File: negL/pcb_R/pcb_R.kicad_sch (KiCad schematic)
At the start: 105 parts, among them J1 MJ-4PP-9, J2 FH-1x4SG/RH, J3 XA-3-2-7P, Q1 AO3401A, SW1 TVBP06-B043CB-B, SW2 EVQWGD001, U1 nice_nano, U2 74HC595, U3 AE-XCL103-3V3

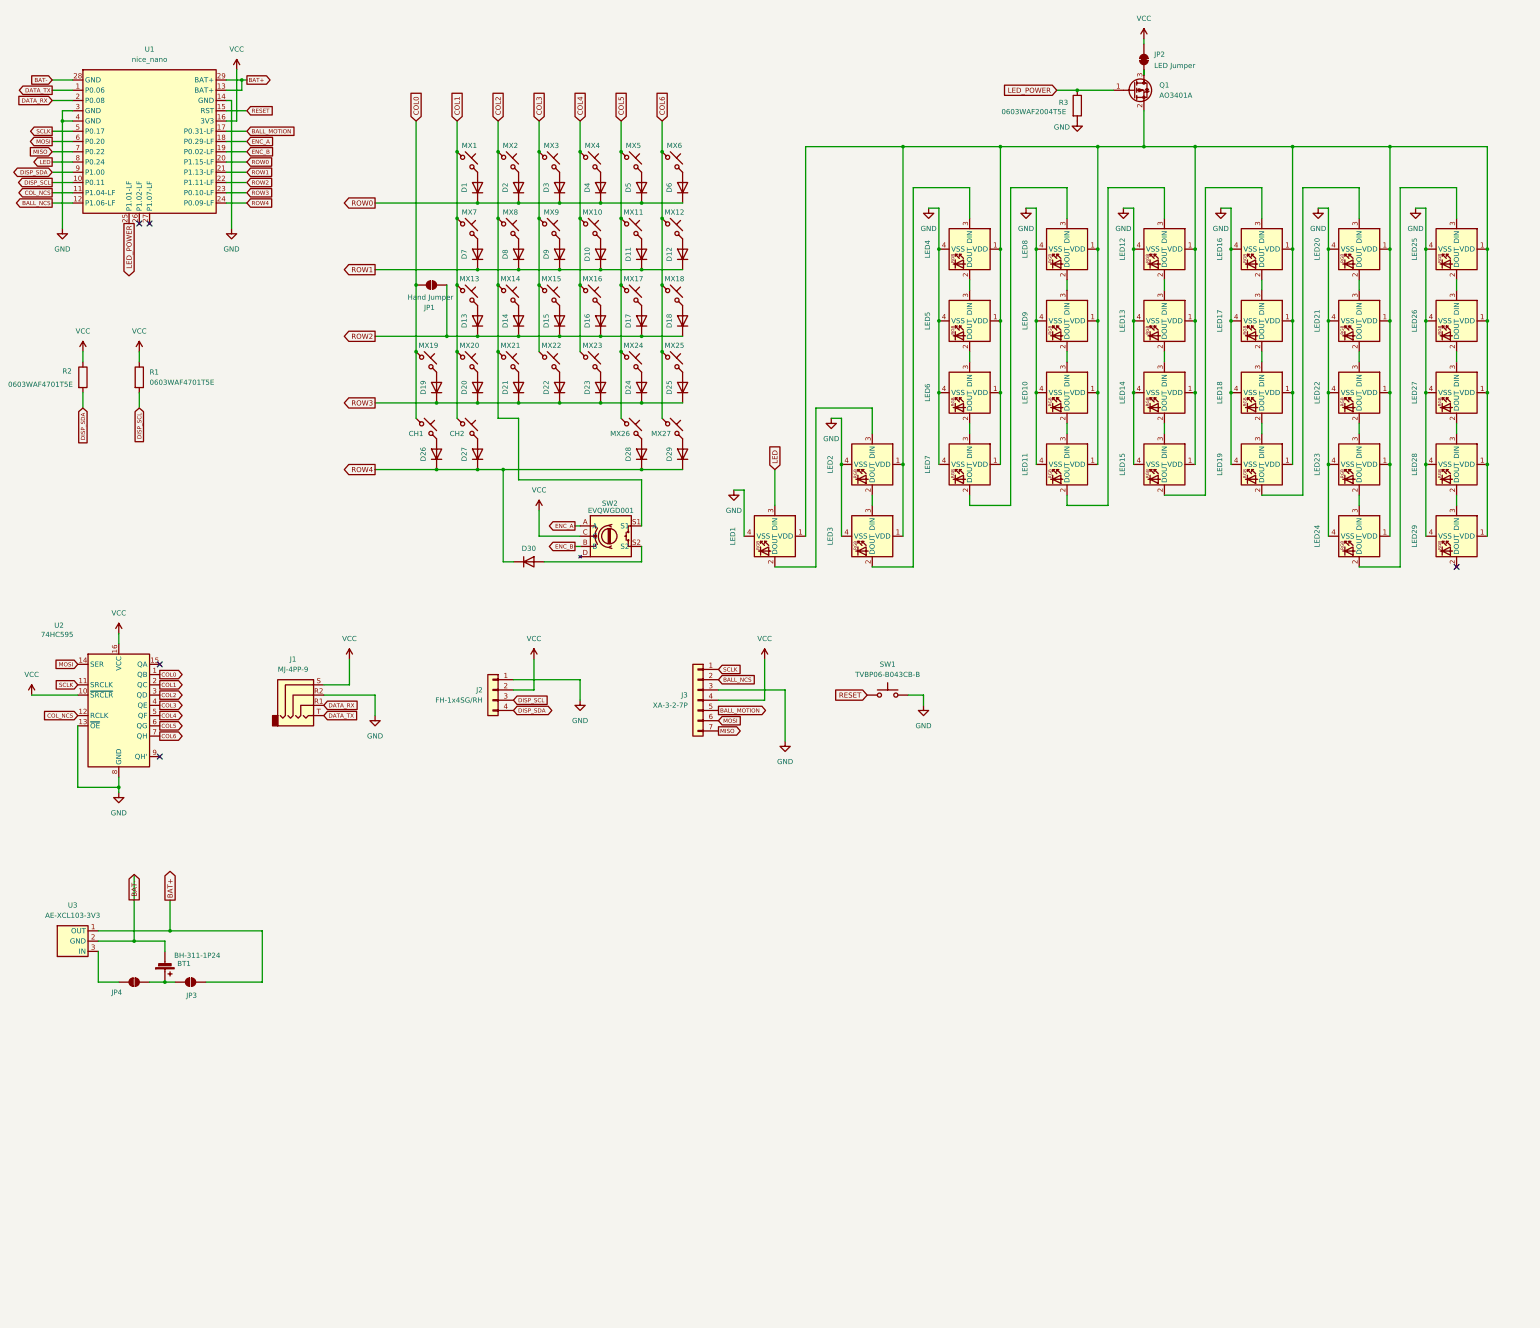
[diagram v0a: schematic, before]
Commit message: Add switches
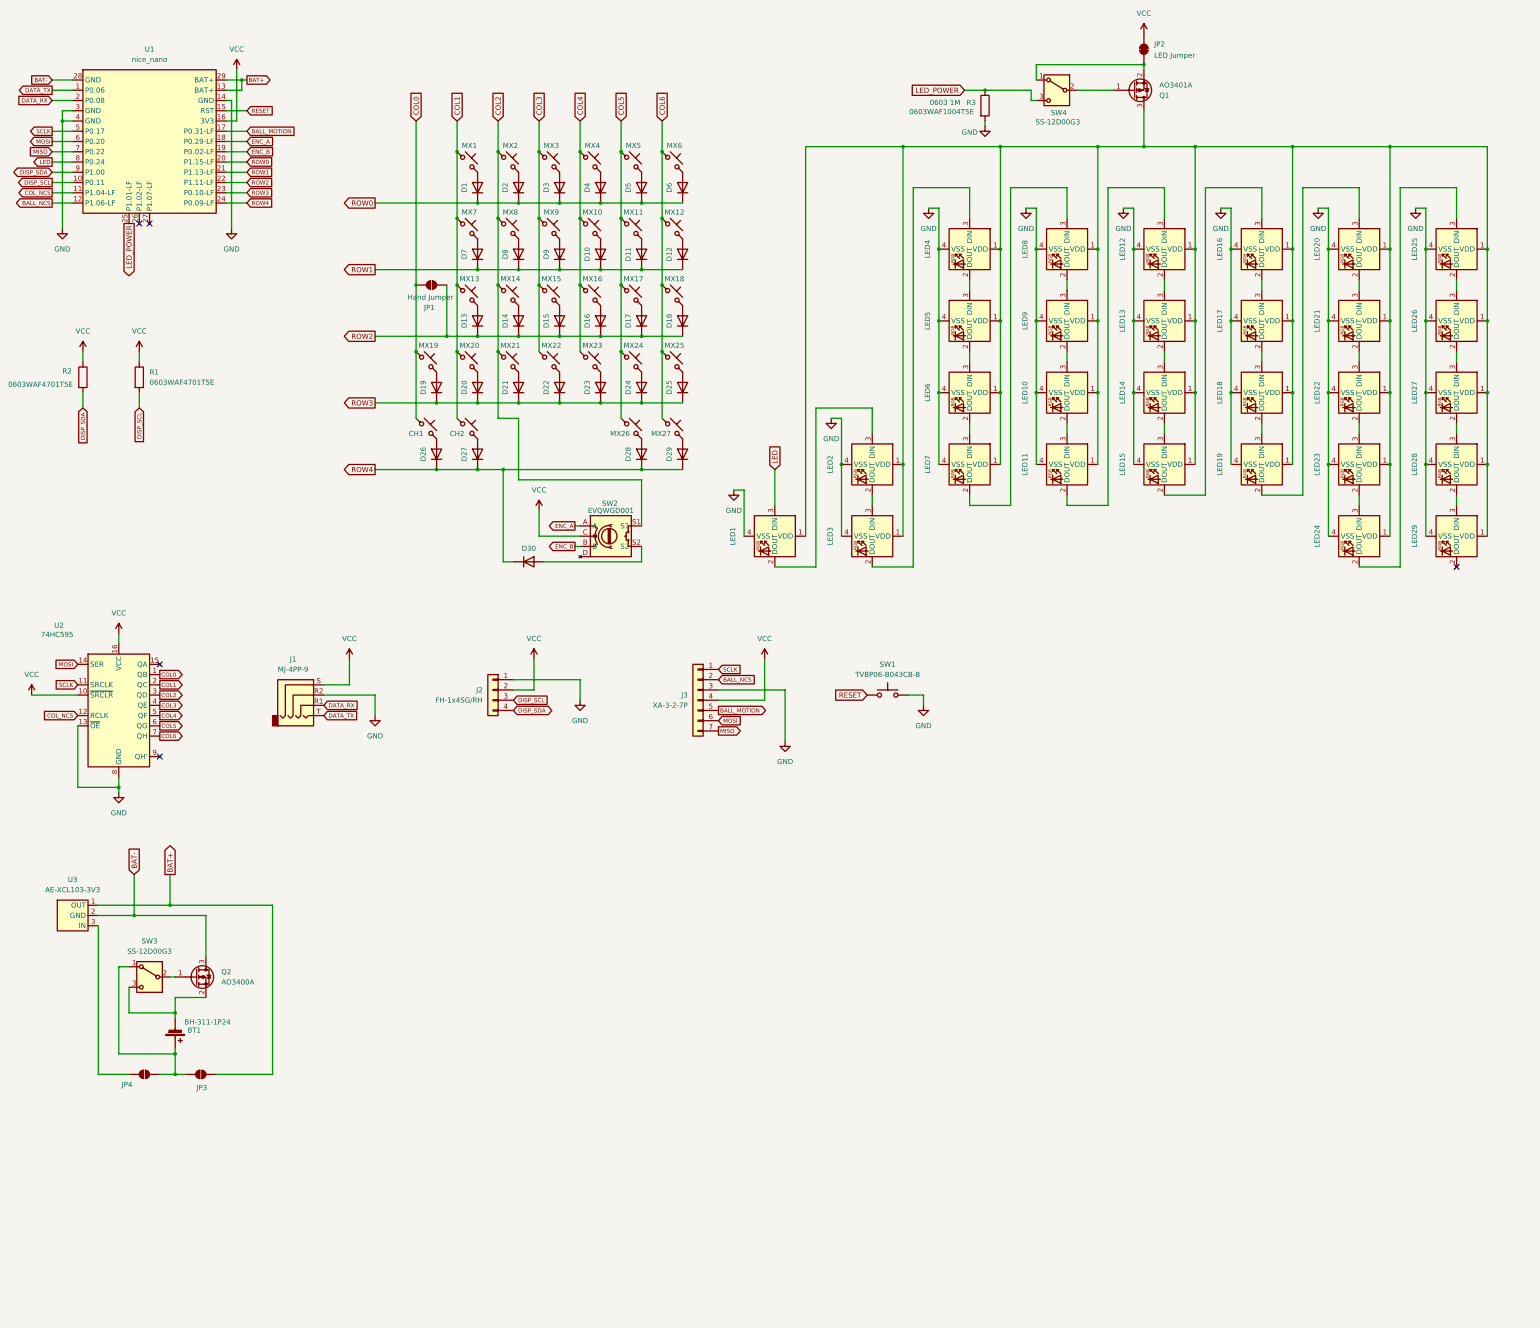
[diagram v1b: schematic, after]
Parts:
- added Q2: AO3400A, Package_TO_SOT_SMD:SOT-23, symbol Transistor_FET:AO3400A
- added SW3, SW4: SS-12D00G3, neg_footprints:SS-12D00G3, symbol Switch:SW_SPDT
- BT1, J1, J2, SW1: now left out of the parts list
- R3: value 0603WAF2004T5E -> 0603WAF1004T5E; LCSC C22976 -> C22935
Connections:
- net BAT-: now also Q2.3 (D); no longer BT1.2 (-)
- net LED_POWER: now also SW4.3 (C); no longer Q1.1 (G)
- net at LED1.1 (VDD), LED10.1 (VDD), LED11.1 (VDD)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: now also Q1.3 (D); no longer Q1.2 (S)
- net at JP2.2 (B): now also Q1.2 (S), SW4.1 (A); no longer Q1.3 (D)
- net at BT1.1 (+), JP3.1 (A), JP4.2 (B): now also SW3.1 (A)
- new net: Q1.1 (G), SW4.2 (B)
- new net: Q2.1 (G), SW3.2 (B)
- new net: BT1.2 (-), Q2.2 (S), SW3.3 (C)
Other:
- moved on the sheet: BT1, JP2, JP3, JP4, R3, U3

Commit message: update
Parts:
- added JP10, JP7, JP8, JP9: ~, Jumper:SolderJumper-2_P1.3mm_Open_Pad1.0x1.5mm, symbol Jumper:SolderJumper_2_Open
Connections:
- net DATA_RX: now also JP10.2 (B), JP7.2 (B); no longer J1.R1
- net DATA_TX: now also JP8.2 (B), JP9.2 (B); no longer J1.T
- new net: J1.R1, JP7.1 (A), JP9.1 (A)
- new net: J1.T, JP10.1 (A), JP8.1 (A)
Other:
- moved on the sheet: J1

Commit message: update
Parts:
- renumbered JP7 to JP5, JP8 to JP6, JP9 to JP7, JP10 to JP8
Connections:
- net COL0: now also U2.15 (QA); no longer MX19.1, U2.1 (QB)
- net COL1: now also MX19.1, U2.1 (QB); no longer MX1.1, MX13.1, MX20.1, MX7.1, U2.2 (QC)
- net COL2: now also MX1.1, MX13.1, MX20.1, MX7.1, U2.2 (QC); no longer MX14.1, MX2.1, MX21.1, MX8.1, U2.3 (QD)
- net COL3: now also MX14.1, MX2.1, MX21.1, MX8.1, U2.3 (QD); no longer MX15.1, MX22.1, MX3.1, MX9.1, U2.4 (QE)
- net COL4: now also MX15.1, MX22.1, MX3.1, MX9.1, U2.4 (QE); no longer MX10.1, MX16.1, MX23.1, MX4.1, U2.5 (QF)
- net COL5: now also MX10.1, MX16.1, MX23.1, MX4.1, U2.5 (QF); no longer MX11.1, MX17.1, MX24.1, MX26.1, MX5.1, U2.6 (QG)
- net COL6: now also MX11.1, MX17.1, MX24.1, MX26.1, MX5.1, U2.6 (QG); no longer MX12.1, MX18.1, MX25.1, MX27.1, MX6.1, U2.7 (QH)
- net ROW2: no longer JP1.2 (B)
- net ROW3: now also JP1.2 (B)
- new net COL7: MX12.1, MX18.1, MX25.1, MX27.1, MX6.1, U2.7 (QH)
- no-connect marks 5 -> 4
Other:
- note added: "JP3: Enables direct output from battery. Intented to use with 14500 battery. JP4: Enables step up converter to 3.3V. Intended to use with normal AA battery."
- note added: "NOTE: XCL103's max current is 0.25A at 1.5V, which is not enough to light all LEDs in max brightness"
- note added: "Short JP7 and JP8 for right hand"
- moved on the sheet: BT1, D30, J1, J2, J3, JP3, JP4, JP5, JP6, JP7, JP8, Q2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

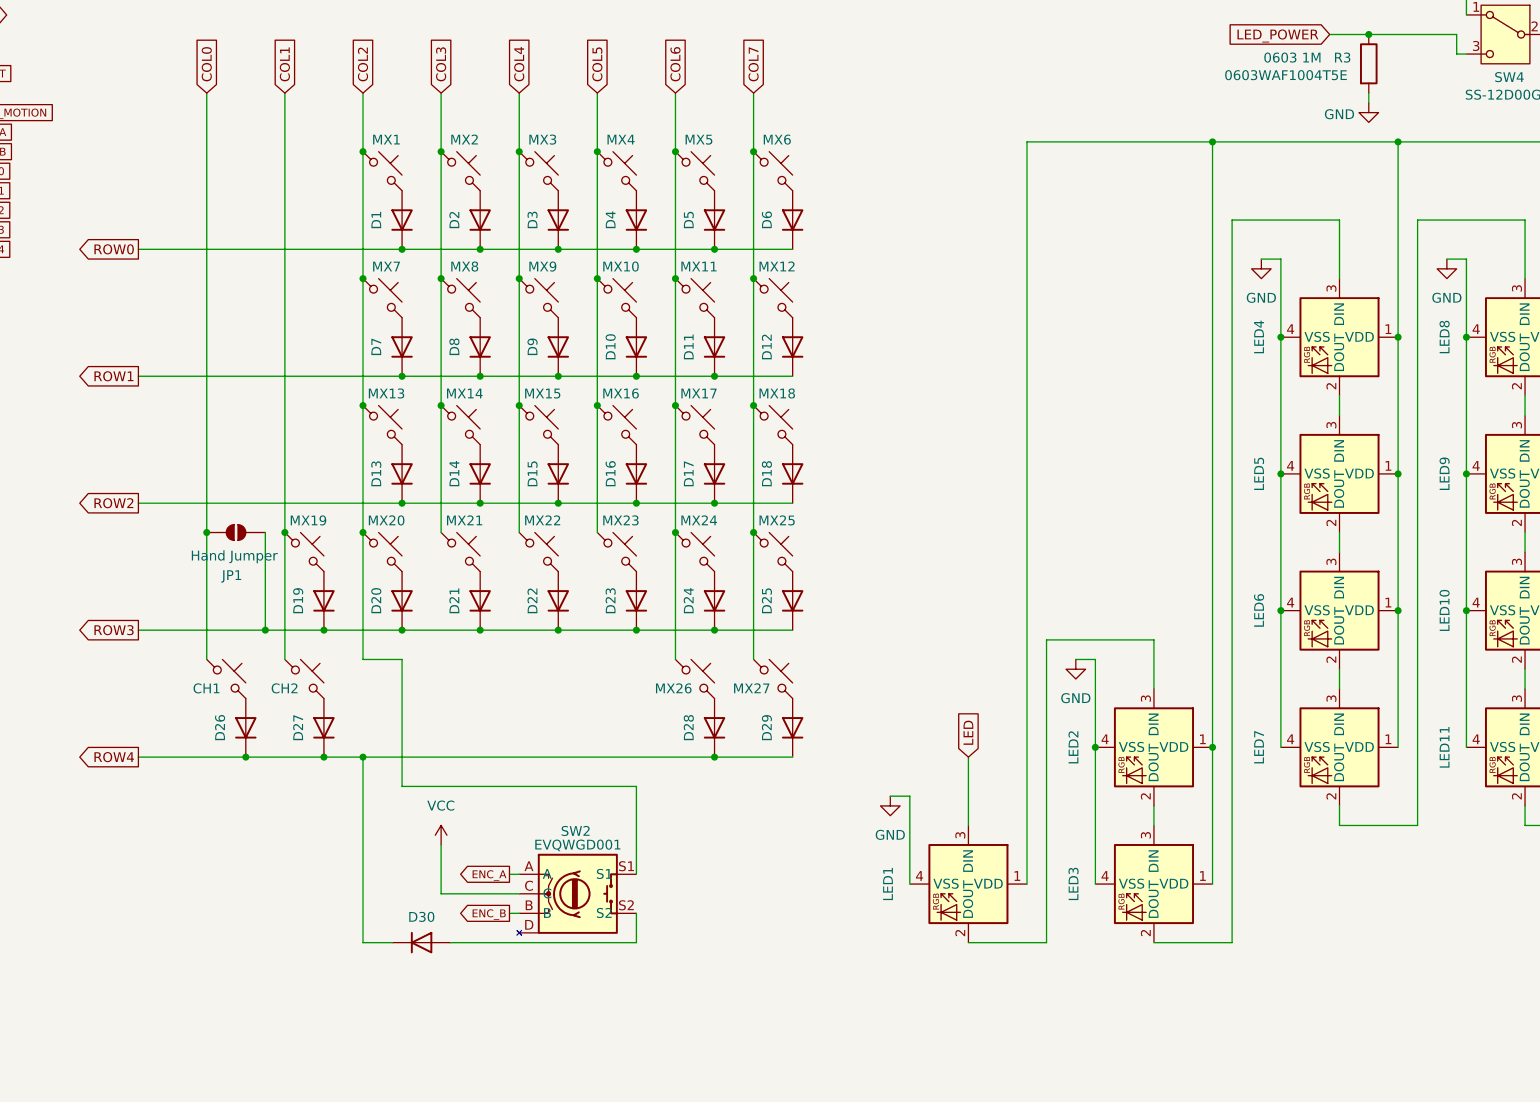
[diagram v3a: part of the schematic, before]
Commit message: change encoder position
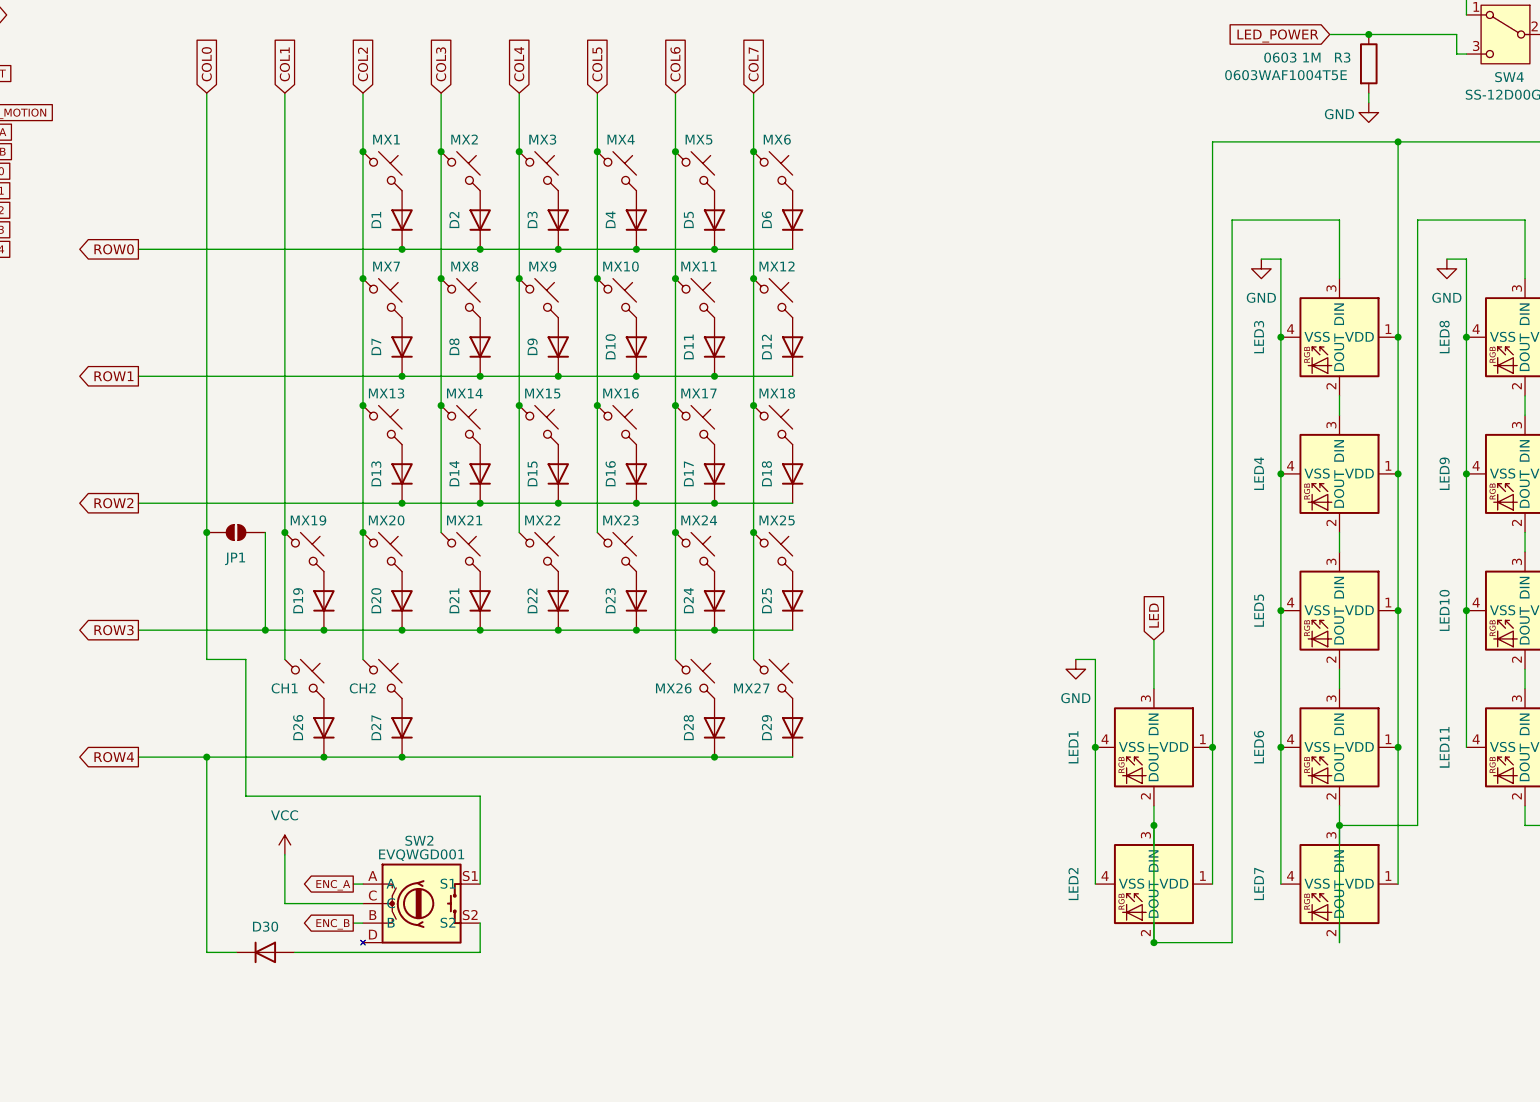
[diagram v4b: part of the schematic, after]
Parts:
- SW2: footprint neg_footprints:RollerEncoder_Panasonic_EVQWGD001 -> neg_footprints:EVQWGD001_EC12
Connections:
- net COL0: now also SW2.S1; no longer CH1.1
- net COL1: now also CH1.1; no longer CH2.1
- net COL2: now also CH2.1; no longer SW2.S1
- net at LED6.2 (DOUT), LED7.3 (DIN): now also LED7.2 (DOUT), LED8.3 (DIN)
- net at LED1.2 (DOUT), LED2.3 (DIN): now also LED2.2 (DOUT), LED3.3 (DIN)
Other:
- moved on the sheet: LED2, LED4, LED5, LED6, LED7

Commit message: update
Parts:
- U1: footprint PCM_marbastlib-xp-promicroish:nice_nano_AH_USBup -> neg_footprints:promicro_nrf
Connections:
- net BAT+: no longer U1.13 (BAT+)
- net at LED3.2 (DOUT): now also LED8.3 (DIN); no longer LED4.3 (DIN)
- net at LED1.2 (DOUT), LED2.3 (DIN): no longer LED2.2 (DOUT), LED3.3 (DIN)
- net at LED6.2 (DOUT), LED7.3 (DIN): no longer LED7.2 (DOUT), LED8.3 (DIN)
- new net: LED3.3 (DIN), LED7.2 (DOUT)
- new net: LED2.2 (DOUT), LED4.3 (DIN)
- no-connect marks 4 -> 5
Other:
- note added: "NOTE: BLE Micro ProではBATは1ピンのみで 下のピンが5V出力ピンとなっているため、 上のピンのみをBAT+として扱う"
- moved on the sheet: LED4, LED5, LED6, LED7

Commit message: update
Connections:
- net BAT+: now also U1.13 (BAT+); no longer U1.29 (BAT+)
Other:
- note added: "NOTE: BLE Micro ProではBAT+の下側が5Vピン(多分VDDH?) なのでそっちにBAT+を繋ぐ(上側は多分VDDで3.6Vまでしか受け付けない!)"
- note removed: "NOTE: BLE Micro ProではBATは1ピンのみで 下のピンが5V出力ピンとなっているため、 上のピンのみをBAT+として扱う"
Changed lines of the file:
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@@
 	)
 	(no_connect
-		(at 73.66 33.02)
-	)
-	(no_connect
 		(at 160.02 226.06)
 	)
@@
 		(at 374.65 151.13)
 	)
+	(no_connect
+		(at 74.93 30.48)
+	)
 	(wire
 		(pts
@@
 	(wire
 		(pts
-			(xy 69.85 33.02) (xy 73.66 33.02)
+			(xy 69.85 33.02) (xy 74.93 33.02)
 		)
 		(stroke
@@
 		)
 	)
-	(text "NOTE: BLE Micro ProではBATは1ピンのみで\n下のピンが5V出力ピンとなっているため、\n上のピンのみをBAT+として扱う"
+	(text "NOTE: BLE Micro ProではBAT+の下側が5Vピン(多分VDDH?)\nなのでそっちにBAT+を繋ぐ(上側は多分VDDで3.6Vまでしか受け付けない!)"
 		(exclude_from_sim no)
 		(at 66.802 17.272 0)
@@
 		)
 	)
+	(global_label "BAT+"
+		(shape output)
+		(at 74.93 33.02 0)
+		(fields_autoplaced yes)
+		(effects
+			(font
+				(size 1.016 1.016)
+			)
+			(justify left)
+		)
+		(property "Intersheetrefs" "${INTERSHEET_REFS}"
+			(at 82.8138 33.02 0)
+			(effects
+				(font
+					(size 1.27 1.27)
+				)
+				(justify left)
+				(hide yes)
+			)
+		)
+	)
 	(global_label "ENC_B"
 		(shape input)
@@
 			(effects
 				(font
-					(size 1.27 1.27)
-				)
-				(justify left)
-				(hide yes)
-			)
-		)
-	)
-	(global_label "BAT+"
-		(shape output)
-		(at 74.93 30.48 0)
-		(fields_autoplaced yes)
-		(effects
-			(font
-				(size 1.016 1.016)
-			)
-			(justify left)
-		)
-		(property "Intersheetrefs" "${INTERSHEET_REFS}"
-			(at 82.8138 30.48 0)
-			(effects
-				(font
